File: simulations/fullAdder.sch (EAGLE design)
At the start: 25 parts

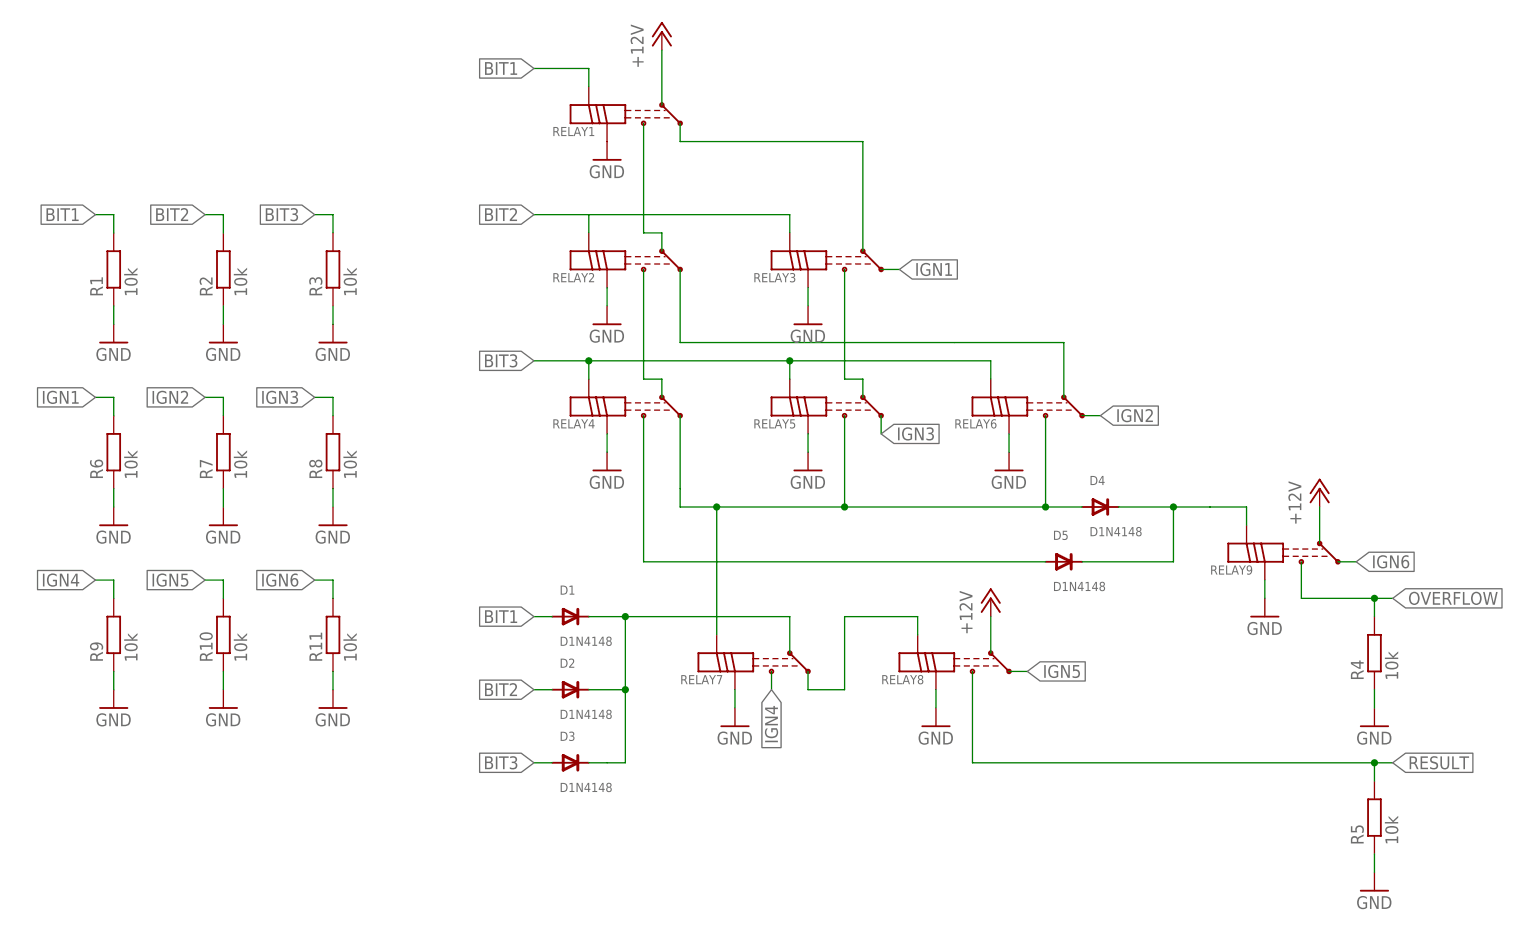
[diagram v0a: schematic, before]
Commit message: Refactoring relay module to include pull-downs
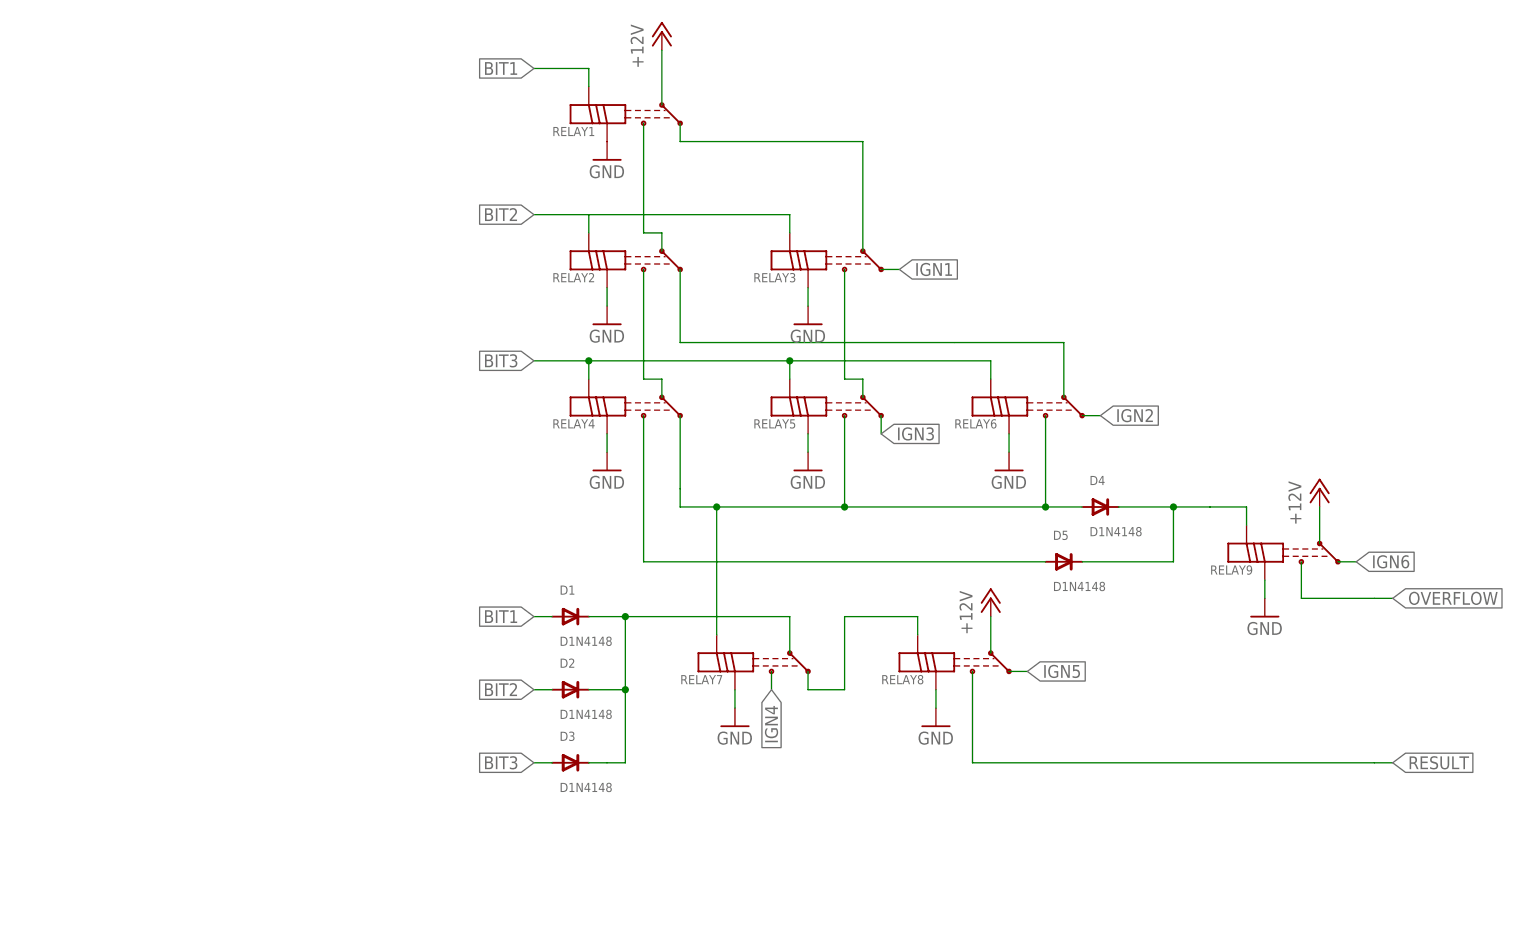
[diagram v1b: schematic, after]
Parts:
- removed R1, R10, R11, R2, R3, R4, R5, R6, R7, R8, R9: 10k, p.peter-scoville.tests:R-EU_R0603
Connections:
- net BIT1: no longer R1.2
- net BIT2: no longer R2.2
- net BIT3: no longer R3.2
- net GND: no longer R1.1, R10.1, R11.1, R2.1, R3.1, R4.1, R5.1, R6.1, R7.1, R8.1, R9.1
- net IGN1: no longer R6.2
- net IGN2: no longer R7.2
- net IGN3: no longer R8.2
- net IGN4: no longer R9.2
- net IGN5: no longer R10.2
- net IGN6: no longer R11.2
- net OVERFLOW: no longer R4.2
- net RESULT: no longer R5.2
